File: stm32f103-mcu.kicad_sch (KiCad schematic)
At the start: 15 parts, among them U7 STM32F103CBUx, Y1 8 MHz

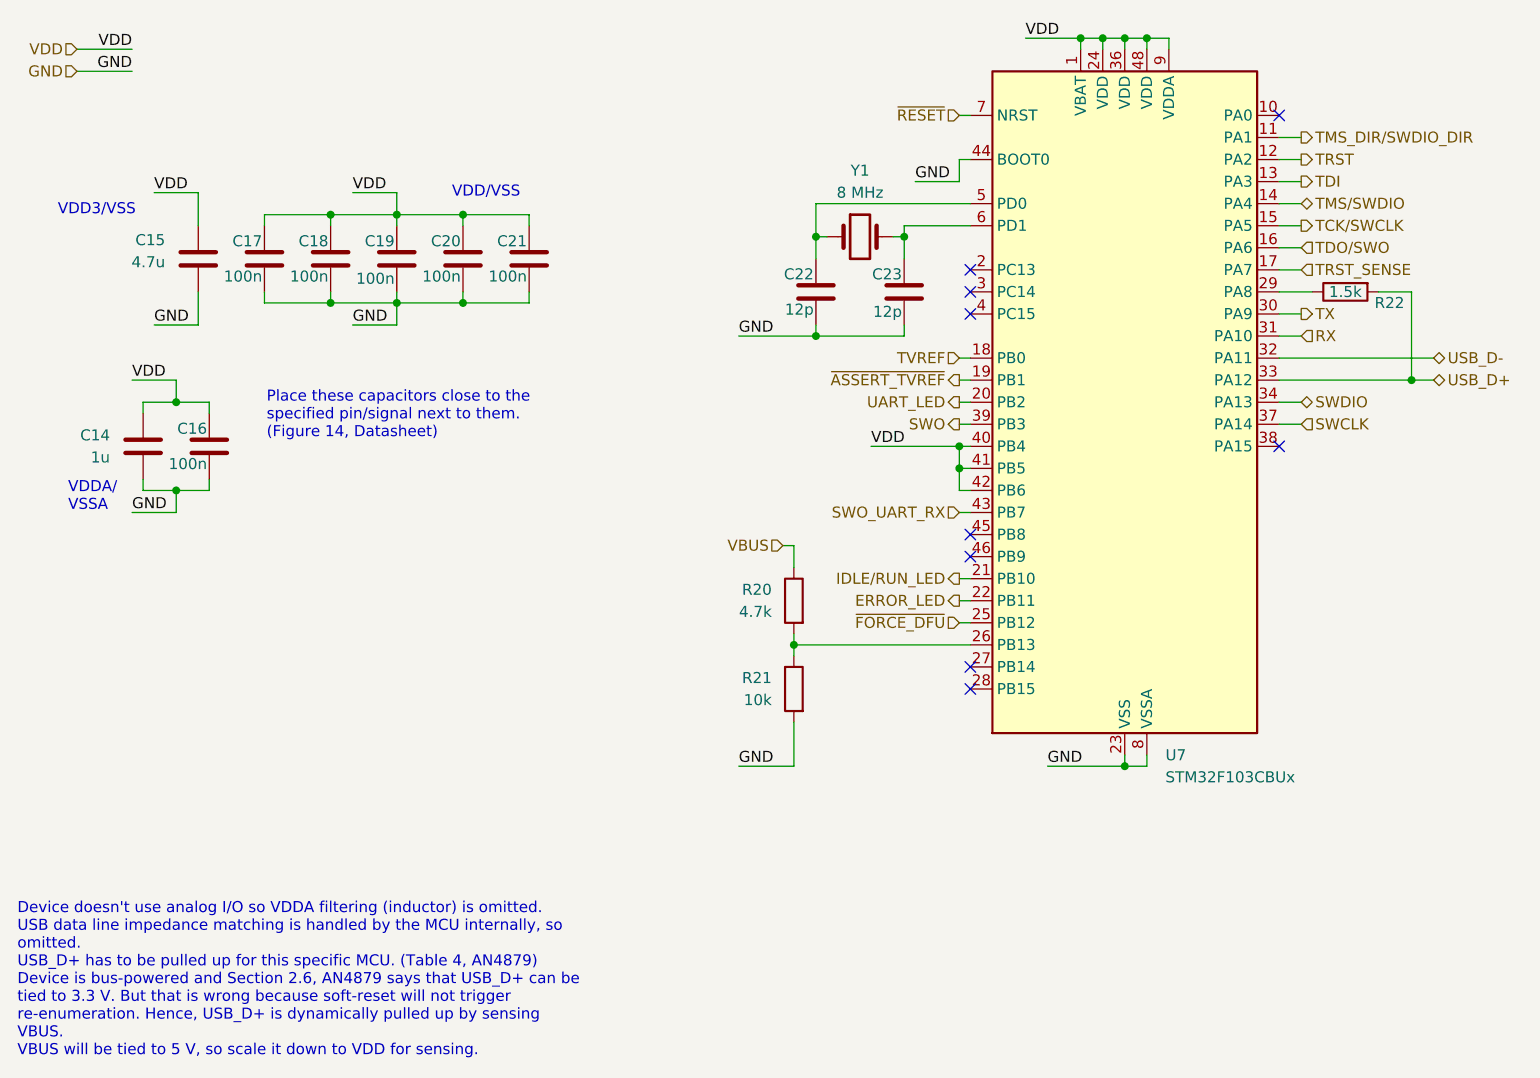
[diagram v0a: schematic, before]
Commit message: layout: initial design with added LCSC part metadata
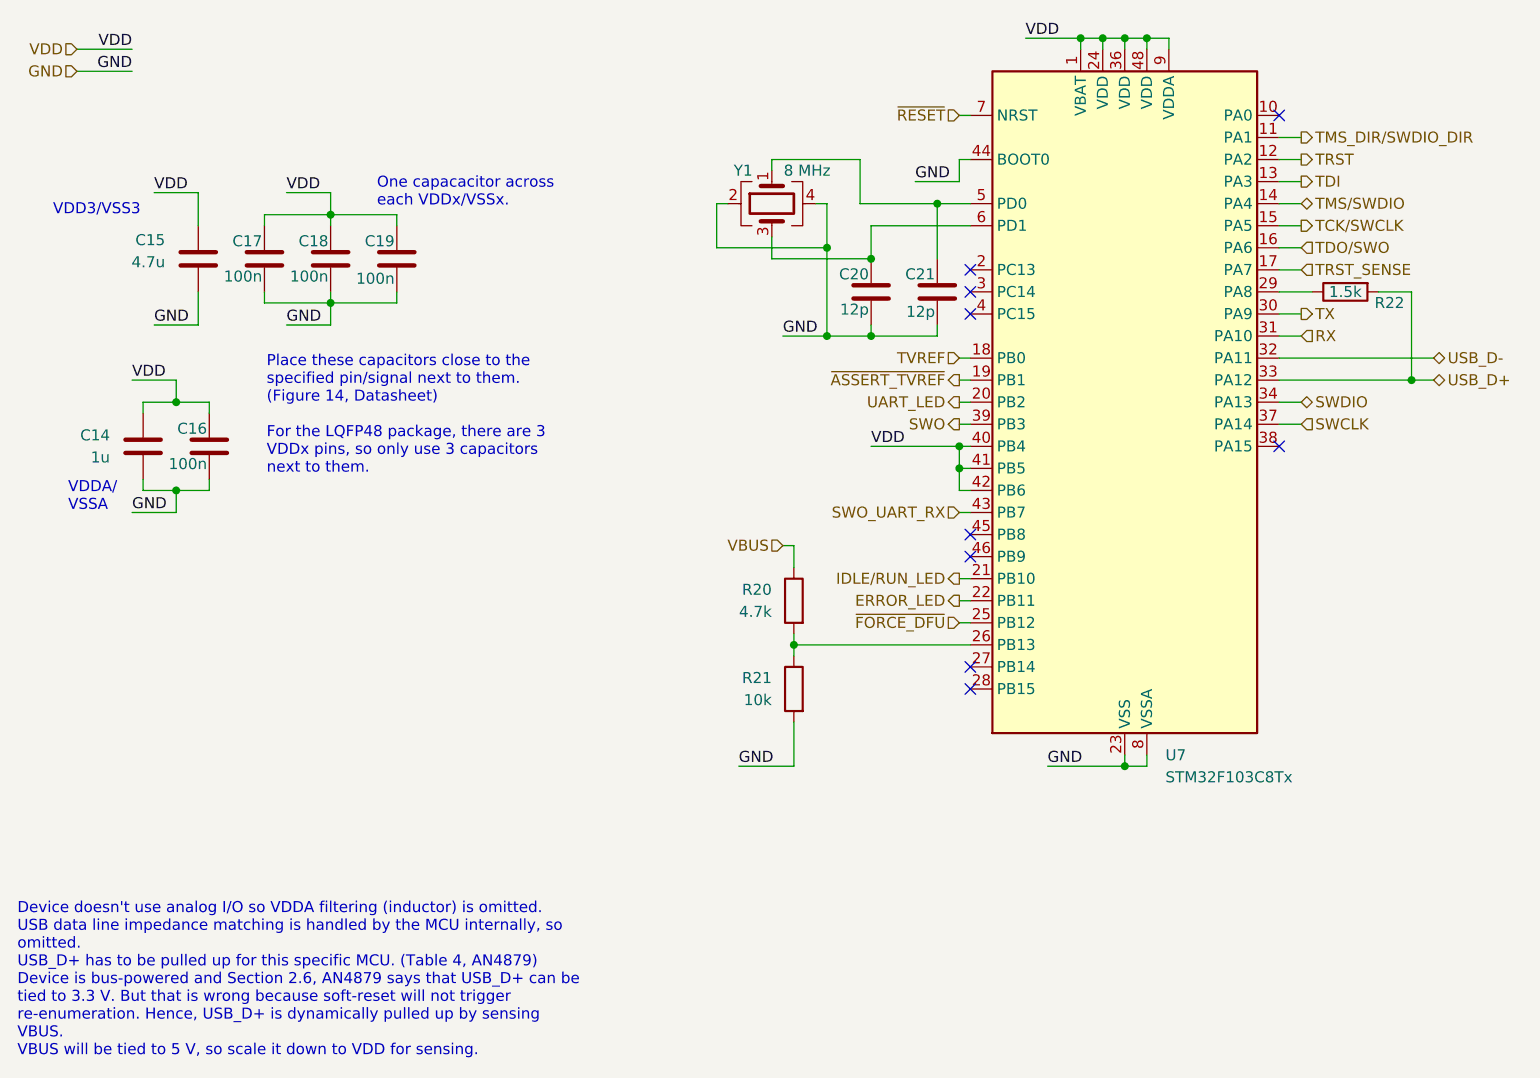
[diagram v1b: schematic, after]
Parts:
- removed C20, C21: 100n, Capacitor_SMD:C_0402_1005Metric, symbol Device:C
- removed U7: STM32F103CBUx, Package_DFN_QFN:QFN-48-1EP_7x7mm_P0.5mm_EP5.6x5.6mm, symbol MCU_ST_STM32F1:STM32F103CBUx
- removed Y1: 8 MHz, Crystal:Crystal_SMD_2016-4Pin_2.0x1.6mm, symbol Device:Crystal
- added U7: STM32F103C8Tx, Package_QFP:LQFP-48_7x7mm_P0.5mm, symbol MCU_ST_STM32F1:STM32F103C8Tx
- added Y1: 8 MHz, footprints:Crystal_4P_GND24, symbol Crystal-4P-GND24:Crystal_4P_GND24
- C14: LCSC Part (none) -> C14445
- C15: LCSC Part (none) -> C23733
- C16, C17, C18, C19: LCSC Part (none) -> C60474
- C20: renamed from C22; LCSC Part (none) -> C106201
- C21: renamed from C23; LCSC Part (none) -> C106201
- R20: footprint Capacitor_SMD:C_0402_1005Metric -> Resistor_SMD:R_0402_1005Metric; LCSC Part (none) -> C105871
- R21: footprint Capacitor_SMD:C_0402_1005Metric -> Resistor_SMD:R_0402_1005Metric; LCSC Part (none) -> C60490
- R22: footprint Capacitor_SMD:C_0402_1005Metric -> Resistor_SMD:R_0402_1005Metric; LCSC Part (none) -> C114759
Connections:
- net ERROR_LED: now also U7.22 (PB11)
- net GND: now also U7.23 (VSS), U7.35 (VSS), U7.44 (BOOT0), U7.47 (VSS), U7.8 (VSSA), Y1.2, Y1.4
- net IDLE/RUN_LED: now also U7.21 (PB10)
- net RX: now also U7.31 (PA10)
- net SWCLK: now also U7.37 (PA14)
- net SWDIO: now also U7.34 (PA13)
- net SWO: now also U7.39 (PB3)
- net SWO_UART_RX: now also U7.43 (PB7)
- net TCK/SWCLK: now also U7.15 (PA5)
- net TDI: now also U7.13 (PA3)
- net TDO/SWO: now also U7.16 (PA6)
- net TMS_DIR/SWDIO_DIR: now also U7.11 (PA1)
- net TMS/SWDIO: now also U7.14 (PA4)
- net TRST: now also U7.12 (PA2)
- net TRST_SENSE: now also U7.17 (PA7)
- net TVREF: now also U7.18 (PB0)
- net TX: now also U7.30 (PA9)
- net UART_LED: now also U7.20 (PB2)
- net USB_D+: now also U7.33 (PA12)
- net USB_D-: now also U7.32 (PA11)
- net VDD: now also U7.1 (VBAT), U7.24 (VDD), U7.36 (VDD), U7.40 (PB4), U7.41 (PB5), U7.42 (PB6), U7.48 (VDD), U7.9 (VDDA)
- net ~{ASSERT_TVREF}: now also U7.19 (PB1)
- net ~{FORCE_DFU}: now also U7.25 (PB12)
- net ~{RESET}: now also U7.7 (NRST)
- net at R20.2, R21.1: now also U7.26 (PB13)
- net at C20.1: now also U7.6 (PD1), Y1.3
- net at C21.1: now also U7.5 (PD0), Y1.1
- net at R22.1: now also U7.29 (PA8)
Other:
- note added: "One capacacitor across each VDDx/VSSx."
- note added: "Place these capacitors close to the specified pin/signal next to them. (Figure 14, Datasheet) For the LQFP48 package, there are 3 VDDx pins, so only use 3 capacitors next to them."
- note added: "VDD3/VSS3"
- note removed: "Place these capacitors close to the specified pin/signal next to them. (Figure 14, Datasheet)"
- note removed: "VDD/VSS"
- note removed: "VDD3/VSS"
- title: Black Magic Probe -> μProbe
- moved on the sheet: C20, C21

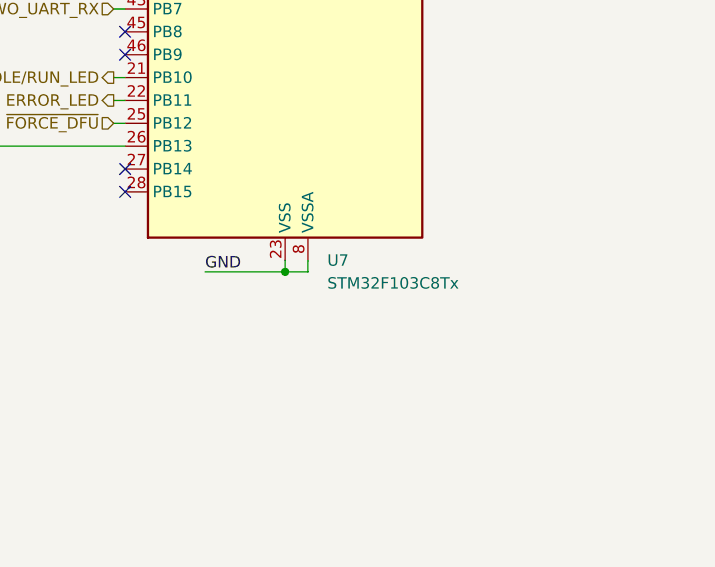
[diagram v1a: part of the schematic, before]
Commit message: schematic: fix C4 LCSC part number and STM32F1 component variant
The BMP firmware cannot be flashed onto the STM32F103C8Tx (64 KiB
variant) due to size constraints. The STM32F103CBUx was used in the
reference schematic but somehow got overlooked during the design.
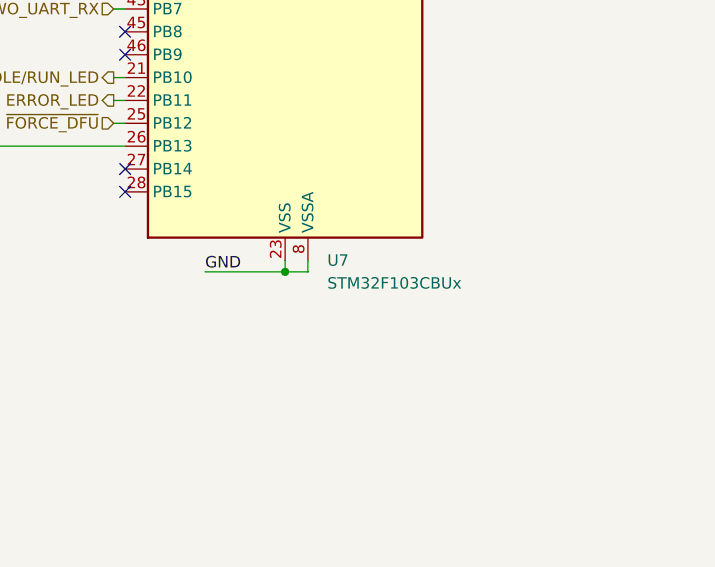
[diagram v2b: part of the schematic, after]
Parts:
- U7: value STM32F103C8Tx -> STM32F103CBUx
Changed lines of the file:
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@@
 			)
 		)
-		(property "Value" "STM32F103C8Tx"
+		(property "Value" "STM32F103CBUx"
 			(at 146.9233 100.33 0)
 			(effects

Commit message: schematic: fix LCSC part number for STM32F1 MCU
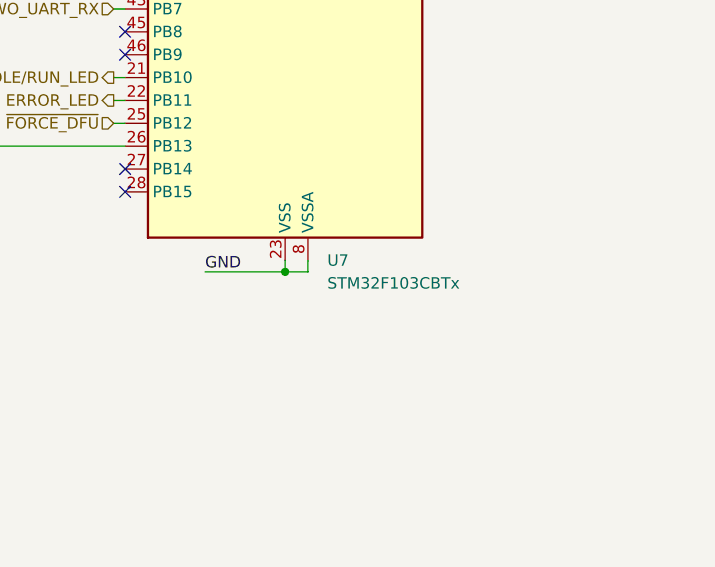
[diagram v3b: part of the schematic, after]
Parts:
- U7: value STM32F103CBUx -> STM32F103CBTx; LCSC Part C8734 -> C8304
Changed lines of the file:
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@@
 			)
 		)
-		(property "Value" "STM32F103CBUx"
+		(property "Value" "STM32F103CBTx"
 			(at 146.9233 100.33 0)
 			(effects
@@
 			)
 		)
-		(property "LCSC Part" "C8734"
+		(property "LCSC Part" "C8304"
 			(at 142.24 57.15 0)
 			(effects
